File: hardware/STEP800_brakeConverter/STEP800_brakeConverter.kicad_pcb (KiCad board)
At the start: 2 copper layers, 11 parts, among them J1 Conn_02x05_Odd_Even, J2 Conn_02x03_Odd_Even, J3 Conn_02x03_Odd_Even, J4 Barrel_Jack_Switch, J5 Conn_01x02, J6 Conn_01x02, J7 Conn_01x02

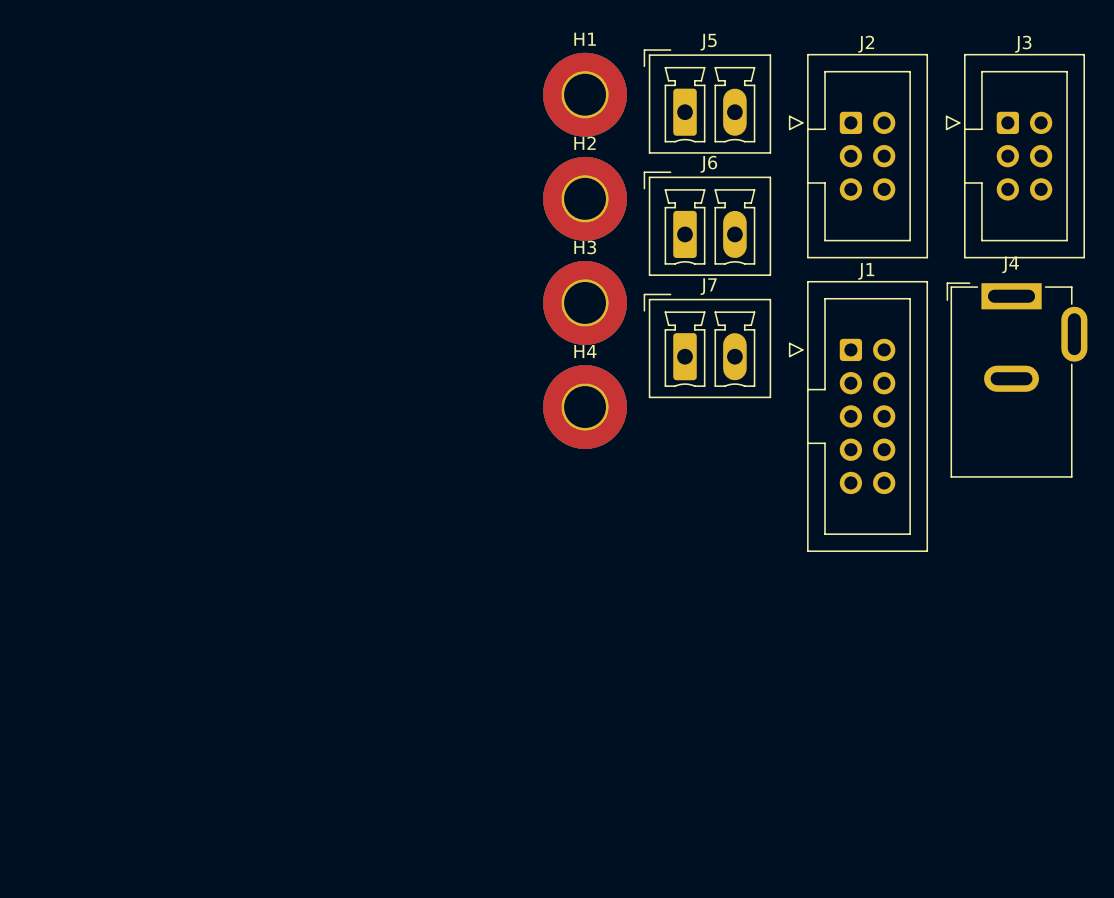
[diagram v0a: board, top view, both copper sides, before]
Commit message: brake board pcb design update
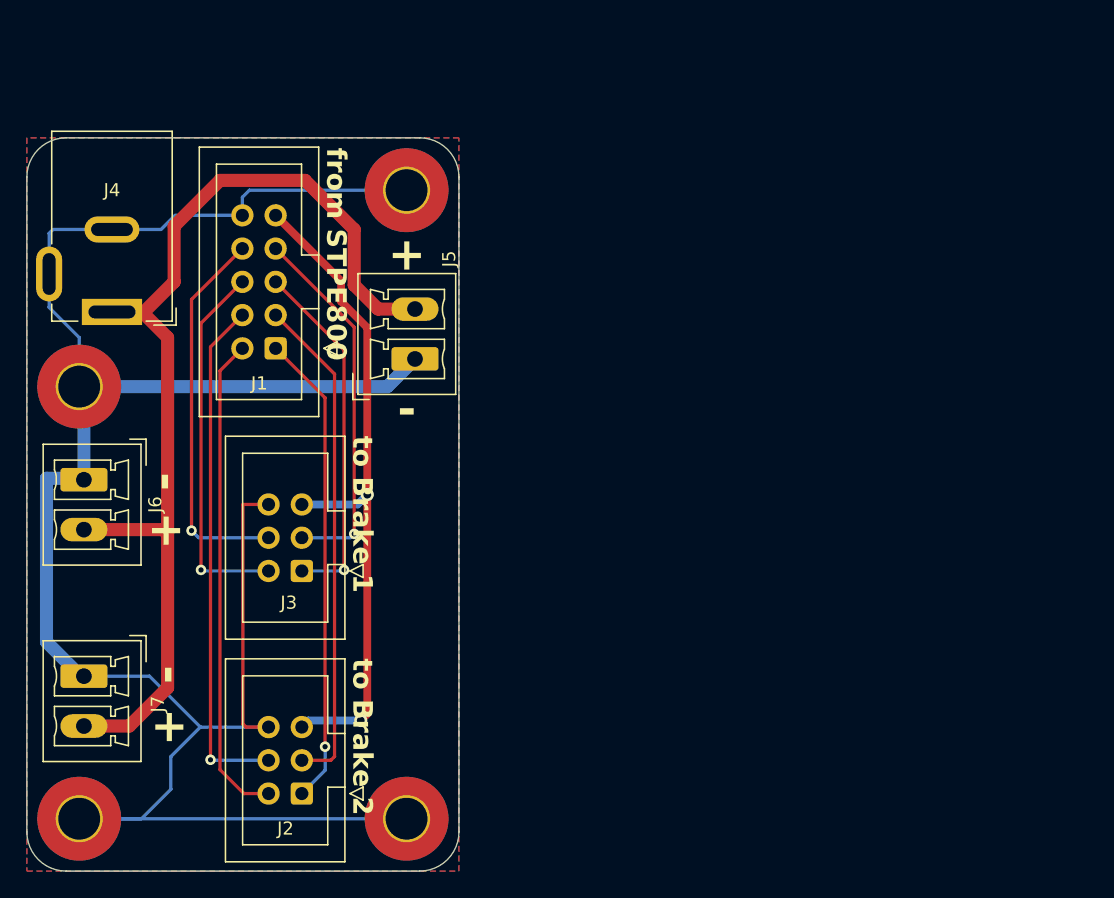
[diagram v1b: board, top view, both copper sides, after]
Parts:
- moved J4 68.7 mm to (86.5, 97.3), turned to 180 degrees
- moved H1 67.4 mm to (84.0, 136.0)
- moved J2 66.2 mm to (101.0, 134.1), turned to 180 degrees
- moved J3 63.9 mm to (101.0, 117.1), turned to 180 degrees
- moved J7 52.0 mm to (84.4, 125.1), turned to -90 degrees
- moved J6 49.6 mm to (84.4, 110.1), turned to -90 degrees
- moved J1 43.9 mm to (99.0, 100.1), turned to 180 degrees
- moved H3 39.2 mm to (84.0, 103.0)
- moved H4 34.3 mm to (109.0, 136.0)
- moved J5 27.9 mm to (109.6, 100.9), turned to 90 degrees
- moved H2 13.6 mm to (109.0, 88.0)
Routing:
- net GND: track 0.00 -> 170.4 mm
- net Net-(J5-Pin_2): track 0.00 -> 82.9 mm
- net +3.3V: track 0.00 -> 51.7 mm, vias 0 -> 2
- net Net-(J1-Pin_4): track 0.00 -> 39.4 mm, vias 0 -> 1
- net Net-(J1-Pin_3): track 0.00 -> 38.2 mm
- net Net-(J1-Pin_2): track 0.00 -> 37.3 mm
- net Net-(J1-Pin_1): track 0.00 -> 36.3 mm, vias 0 -> 1
- net Net-(J1-Pin_8): track 0.00 -> 29.3 mm, vias 0 -> 1
- net Net-(J1-Pin_6): track 0.00 -> 28.5 mm, vias 0 -> 1
- net Net-(J1-Pin_7): track 0.00 -> 28.4 mm, vias 0 -> 1
- net Net-(J1-Pin_5): track 0.00 -> 27.4 mm, vias 0 -> 1
- added copper zone on B.Cu, net GND
- added copper zone on F.Cu, net GND
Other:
- board outline added: 33 x 56 mm
- board text added: "+"
- board text added: "-"
- board text added: "from STPE800"
- board text added: "to Brake 1"
- board text added: "to Brake 2"

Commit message: brake conv gerber data for the prototype
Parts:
- added G***: LOGO, STEP800_brakeConverter_Library:ponoor_full_21x6, F.Cu at (109.5, 120.8)
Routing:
- net Net-(J5-Pin_2): track 82.9 -> 73.7 mm
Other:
- board text added: "Brake Converter Board for STEP800 rev. 0.0.1 / 2023-03-23 info@ponoor.com"
- board text added: "Vin"
- board text added: "Vout"
